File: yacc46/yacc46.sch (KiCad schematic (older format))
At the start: 127 parts, among them J1 CX70M-24P1, J2 OLED_I2C, J3 AVR-ISP-6, J4 GLOVE_I2C, J5 TRRS_I2C, SW1 SW_PUSH, SW10 SW_PUSH, SW11 SW_PUSH, SW12 SW_PUSH, SW13 SW_PUSH, SW14 SW_PUSH, SW15 SW_PUSH, SW16 SW_PUSH, SW17 SW_PUSH, SW18 SW_PUSH, SW19 Rotary_Encoder_Switch, SW2 SW_PUSH, SW20 SW_PUSH, SW21 SW_PUSH, SW22 SW_PUSH, SW23 SW_PUSH, SW24 SW_PUSH, SW25 SW_PUSH, SW26 SW_PUSH, SW27 SW_PUSH, SW28 SW_PUSH, SW29 SW_PUSH, SW3 SW_PUSH, SW30 SW_PUSH, SW31 SW_PUSH, SW32 SW_PUSH, SW33 SW_PUSH, SW34 SW_PUSH, SW35 SW_PUSH, SW36 Rotary_Encoder_Switch, SW37 SW_PUSH, SW38 SW_PUSH, SW39 SW_PUSH, SW4 SW_PUSH, SW40 SW_PUSH, SW41 SW_PUSH, SW42 SW_PUSH, SW43 SW_PUSH, SW44 SW_PUSH, SW45 SW_PUSH, SW46 SW_PUSH, SW47 SW_Push, SW5 SW_PUSH, SW6 SW_PUSH, SW7 SW_PUSH, SW8 SW_PUSH, SW9 SW_PUSH, U1 ATmega32U4-AU, Y1 16MHz

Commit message: リセットスイッチ・水晶のフットプリントを変更
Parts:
- SW47: footprint 1m38_kbd:ResetSW_SKRPABE010 -> 1m38_kbd:SW_PUSH_SMD_TVAF06-A020B-R_HandSolder
- Y1: footprint Crystal:Crystal_SMD_2520-4Pin_2.5x2.0mm -> Crystal:Crystal_SMD_SeikoEpson_FA238-4Pin_3.2x2.5mm_HandSoldering
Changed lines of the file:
@@
 F 0 "SW47" H 3300 6085 50  0000 C CNN
 F 1 "SW_Push" H 3300 5994 50  0000 C CNN
-F 2 "1m38_kbd:ResetSW_SKRPABE010" H 3300 6000 50  0001 C CNN
+F 2 "1m38_kbd:SW_PUSH_SMD_TVAF06-A020B-R_HandSolder" H 3300 6000 50  0001 C CNN
 F 3 "~" H 3300 6000 50  0001 C CNN
 	1    3300 5800
@@
 F 0 "Y1" V 1654 6194 50  0000 L CNN
 F 1 "16MHz" V 1745 6194 50  0000 L CNN
-F 2 "Crystal:Crystal_SMD_2520-4Pin_2.5x2.0mm" H 1700 5950 50  0001 C CNN
+F 2 "Crystal:Crystal_SMD_SeikoEpson_FA238-4Pin_3.2x2.5mm_HandSoldering" H 1700 5950 50  0001 C CNN
 F 3 "~" H 1700 5950 50  0001 C CNN
 	1    1700 5950

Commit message: 配線を修正
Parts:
- removed J5: TRRS_I2C, 1m38_kbd:MJ-4PP-9_1side_no-mask, symbol foostan_kbd:MJ-4PP-9
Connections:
- wire segments 345 -> 338
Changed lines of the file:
@@
 encoding utf-8
 Sheet 1 1
-Title ""
+Title "yacc46"
 Date ""
-Rev ""
+Rev "0.2"
 Comp ""
 Comment1 ""
@@
 U 1 1 5F59CB24
 P 1700 5950
-F 0 "Y1" V 1654 6194 50  0000 L CNN
-F 1 "16MHz" V 1745 6194 50  0000 L CNN
+F 0 "Y1" V 1650 5600 50  0000 L CNN
+F 1 "16MHz" V 1750 5450 50  0000 L CNN
 F 2 "Crystal:Crystal_SMD_SeikoEpson_FA238-4Pin_3.2x2.5mm_HandSoldering" H 1700 5950 50  0001 C CNN
 F 3 "~" H 1700 5950 50  0001 C CNN
 	1    1700 5950
-	0    1    1    0
-$EndComp
-Connection ~ 1700 5800
-Connection ~ 1700 6100
+	0    -1   -1   0
+$EndComp
 Wire Wire Line
 	1050 5150 1150 5150
@@
 Wire Wire Line
 	1450 5150 2000 5150
-Wire Wire Line
-	1450 5800 1700 5800
-Wire Wire Line
-	1450 6100 1700 6100
-Wire Wire Line
-	1700 5800 2000 5800
-Wire Wire Line
-	1700 6100 2000 6100
 Wire Wire Line
 	1050 6300 1500 6300
@@
 	-1   0    0    1
 $EndComp
-$Comp
-L power:GND #PWR0101
-U 1 1 60A4B503
-P 1900 10250
-F 0 "#PWR0101" H 1900 10000 50  0001 C CNN
-F 1 "GND" H 1905 10077 50  0000 C CNN
-F 2 "" H 1900 10250 50  0001 C CNN
-F 3 "" H 1900 10250 50  0001 C CNN
-	1    1900 10250
-	1    0    0    -1
-$EndComp
-Wire Wire Line
-	1500 10250 1900 10250
-$Comp
-L power:VCC #PWR0102
-U 1 1 60A83F5C
-P 1800 10200
-F 0 "#PWR0102" H 1800 10050 50  0001 C CNN
-F 1 "VCC" H 1815 10373 50  0000 C CNN
-F 2 "" H 1800 10200 50  0001 C CNN
-F 3 "" H 1800 10200 50  0001 C CNN
-	1    1800 10200
-	1    0    0    -1
-$EndComp
-Wire Wire Line
-	1500 10300 1800 10300
-Wire Wire Line
-	1800 10300 1800 10200
-Text GLabel 1600 10350 2    50   Input ~ 0
-SCL
-Text GLabel 1600 10450 2    50   Input ~ 0
-SDA
-Wire Wire Line
-	1500 10350 1600 10350
-Wire Wire Line
-	1500 10400 1550 10400
-Wire Wire Line
-	1550 10400 1550 10450
-Wire Wire Line
-	1550 10450 1600 10450
 Text GLabel 11150 4900 1    50   Input ~ 0
 COL0
@@
 Wire Wire Line
 	11150 2600 11150 3400
-$Comp
-L foostan_kbd:MJ-4PP-9 J5
-U 1 1 60A4AE0C
-P 1300 10325
-F 0 "J5" H 1331 10601 50  0000 C CNN
-F 1 "TRRS_I2C" H 1331 10510 50  0000 C CNN
-F 2 "1m38_kbd:MJ-4PP-9_1side_no-mask" H 1575 10500 50  0001 C CNN
-F 3 "~" H 1575 10500 50  0001 C CNN
-	1    1300 10325
-	1    0    0    -1
-$EndComp
 Text GLabel 2800 8900 3    50   Input ~ 0
 SCL
@@
 Wire Wire Line
 	2750 2350 2750 2550
+Wire Wire Line
+	1450 5800 1700 5800
+Wire Wire Line
+	1450 6100 1700 6100
+Connection ~ 1700 6100
+Wire Wire Line
+	1700 6100 2000 6100
+Connection ~ 1700 5800
+Wire Wire Line
+	1700 5800 2000 5800
 $EndSCHEMATC

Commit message: key_arrange.pyを変更、フットプリントの位置を微調整
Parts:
- C1, C2, C3, C4: footprint Capacitor_SMD:C_0805_2012Metric_Pad1.15x1.40mm_HandSolder -> Capacitor_SMD:C_0805_2012Metric_Pad1.18x1.45mm_HandSolder
- C5, C6: footprint Capacitor_SMD:C_0603_1608Metric_Pad1.05x0.95mm_HandSolder -> Capacitor_SMD:C_0603_1608Metric_Pad1.08x0.95mm_HandSolder
- R1, R2, R3, R4, R5, R6: footprint Resistor_SMD:R_0805_2012Metric_Pad1.15x1.40mm_HandSolder -> Resistor_SMD:R_0805_2012Metric_Pad1.20x1.40mm_HandSolder
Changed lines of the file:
@@
 F 0 "R3" V 2743 3450 50  0000 C CNN
 F 1 "22" V 2834 3450 50  0000 C CNN
-F 2 "Resistor_SMD:R_0805_2012Metric_Pad1.15x1.40mm_HandSolder" V 2880 3450 50  0001 C CNN
+F 2 "Resistor_SMD:R_0805_2012Metric_Pad1.20x1.40mm_HandSolder" V 2880 3450 50  0001 C CNN
 F 3 "~" H 2950 3450 50  0001 C CNN
 	1    2950 3450
@@
 F 0 "R1" V 2743 2050 50  0000 C CNN
 F 1 "5.1k" V 2834 2050 50  0000 C CNN
-F 2 "Resistor_SMD:R_0805_2012Metric_Pad1.15x1.40mm_HandSolder" V 2880 2050 50  0001 C CNN
+F 2 "Resistor_SMD:R_0805_2012Metric_Pad1.20x1.40mm_HandSolder" V 2880 2050 50  0001 C CNN
 F 3 "~" H 2950 2050 50  0001 C CNN
 	1    2950 2050
@@
 F 0 "C5" V 1048 5800 50  0000 C CNN
 F 1 "22p" V 1139 5800 50  0000 C CNN
-F 2 "Capacitor_SMD:C_0603_1608Metric_Pad1.05x0.95mm_HandSolder" H 1338 5650 50  0001 C CNN
+F 2 "Capacitor_SMD:C_0603_1608Metric_Pad1.08x0.95mm_HandSolder" H 1338 5650 50  0001 C CNN
 F 3 "~" H 1300 5800 50  0001 C CNN
 	1    1300 5800
@@
 F 0 "C6" V 1048 6100 50  0000 C CNN
 F 1 "22p" V 1139 6100 50  0000 C CNN
-F 2 "Capacitor_SMD:C_0603_1608Metric_Pad1.05x0.95mm_HandSolder" H 1338 5950 50  0001 C CNN
+F 2 "Capacitor_SMD:C_0603_1608Metric_Pad1.08x0.95mm_HandSolder" H 1338 5950 50  0001 C CNN
 F 3 "~" H 1300 6100 50  0001 C CNN
 	1    1300 6100
@@
 F 0 "C4" V 1448 5450 50  0000 C CNN
 F 1 "1u" V 1539 5450 50  0000 C CNN
-F 2 "Capacitor_SMD:C_0805_2012Metric_Pad1.15x1.40mm_HandSolder" H 1738 5300 50  0001 C CNN
+F 2 "Capacitor_SMD:C_0805_2012Metric_Pad1.18x1.45mm_HandSolder" H 1738 5300 50  0001 C CNN
 F 3 "~" H 1700 5450 50  0001 C CNN
 	1    1700 5450
@@
 F 0 "R5" H 3480 5546 50  0000 R CNN
 F 1 "10k" H 3480 5455 50  0000 R CNN
-F 2 "Resistor_SMD:R_0805_2012Metric_Pad1.15x1.40mm_HandSolder" V 3480 5500 50  0001 C CNN
+F 2 "Resistor_SMD:R_0805_2012Metric_Pad1.20x1.40mm_HandSolder" V 3480 5500 50  0001 C CNN
 F 3 "~" H 3550 5500 50  0001 C CNN
 	1    3550 5500
@@
 F 0 "C3" V 1048 5150 50  0000 C CNN
 F 1 "0.1u" V 1139 5150 50  0000 C CNN
-F 2 "Capacitor_SMD:C_0805_2012Metric_Pad1.15x1.40mm_HandSolder" H 1338 5000 50  0001 C CNN
+F 2 "Capacitor_SMD:C_0805_2012Metric_Pad1.18x1.45mm_HandSolder" H 1338 5000 50  0001 C CNN
 F 3 "~" H 1300 5150 50  0001 C CNN
 	1    1300 5150
@@
 F 0 "R6" V 3093 6150 50  0000 C CNN
 F 1 "10k" V 3184 6150 50  0000 C CNN
-F 2 "Resistor_SMD:R_0805_2012Metric_Pad1.15x1.40mm_HandSolder" V 3230 6150 50  0001 C CNN
+F 2 "Resistor_SMD:R_0805_2012Metric_Pad1.20x1.40mm_HandSolder" V 3230 6150 50  0001 C CNN
 F 3 "~" H 3300 6150 50  0001 C CNN
 	1    3300 6150
@@
 F 0 "C1" H 1335 4104 50  0000 R CNN
 F 1 "10u" H 1335 4195 50  0000 R CNN
-F 2 "Capacitor_SMD:C_0805_2012Metric_Pad1.15x1.40mm_HandSolder" H 1488 4000 50  0001 C CNN
+F 2 "Capacitor_SMD:C_0805_2012Metric_Pad1.18x1.45mm_HandSolder" H 1488 4000 50  0001 C CNN
 F 3 "~" H 1450 4150 50  0001 C CNN
 	1    1450 4150
@@
 F 0 "C2" H 1735 4104 50  0000 R CNN
 F 1 "0.1u" H 1735 4195 50  0000 R CNN
-F 2 "Capacitor_SMD:C_0805_2012Metric_Pad1.15x1.40mm_HandSolder" H 1888 4000 50  0001 C CNN
+F 2 "Capacitor_SMD:C_0805_2012Metric_Pad1.18x1.45mm_HandSolder" H 1888 4000 50  0001 C CNN
 F 3 "~" H 1850 4150 50  0001 C CNN
 	1    1850 4150
@@
 F 0 "R4" V 2743 3750 50  0000 C CNN
 F 1 "22" V 2834 3750 50  0000 C CNN
-F 2 "Resistor_SMD:R_0805_2012Metric_Pad1.15x1.40mm_HandSolder" V 2880 3750 50  0001 C CNN
+F 2 "Resistor_SMD:R_0805_2012Metric_Pad1.20x1.40mm_HandSolder" V 2880 3750 50  0001 C CNN
 F 3 "~" H 2950 3750 50  0001 C CNN
 	1    2950 3750
@@
 F 0 "R2" V 643 2350 50  0000 C CNN
 F 1 "5.1k" V 734 2350 50  0000 C CNN
-F 2 "Resistor_SMD:R_0805_2012Metric_Pad1.15x1.40mm_HandSolder" V 780 2350 50  0001 C CNN
+F 2 "Resistor_SMD:R_0805_2012Metric_Pad1.20x1.40mm_HandSolder" V 780 2350 50  0001 C CNN
 F 3 "~" H 850 2350 50  0001 C CNN
 	1    850  2350

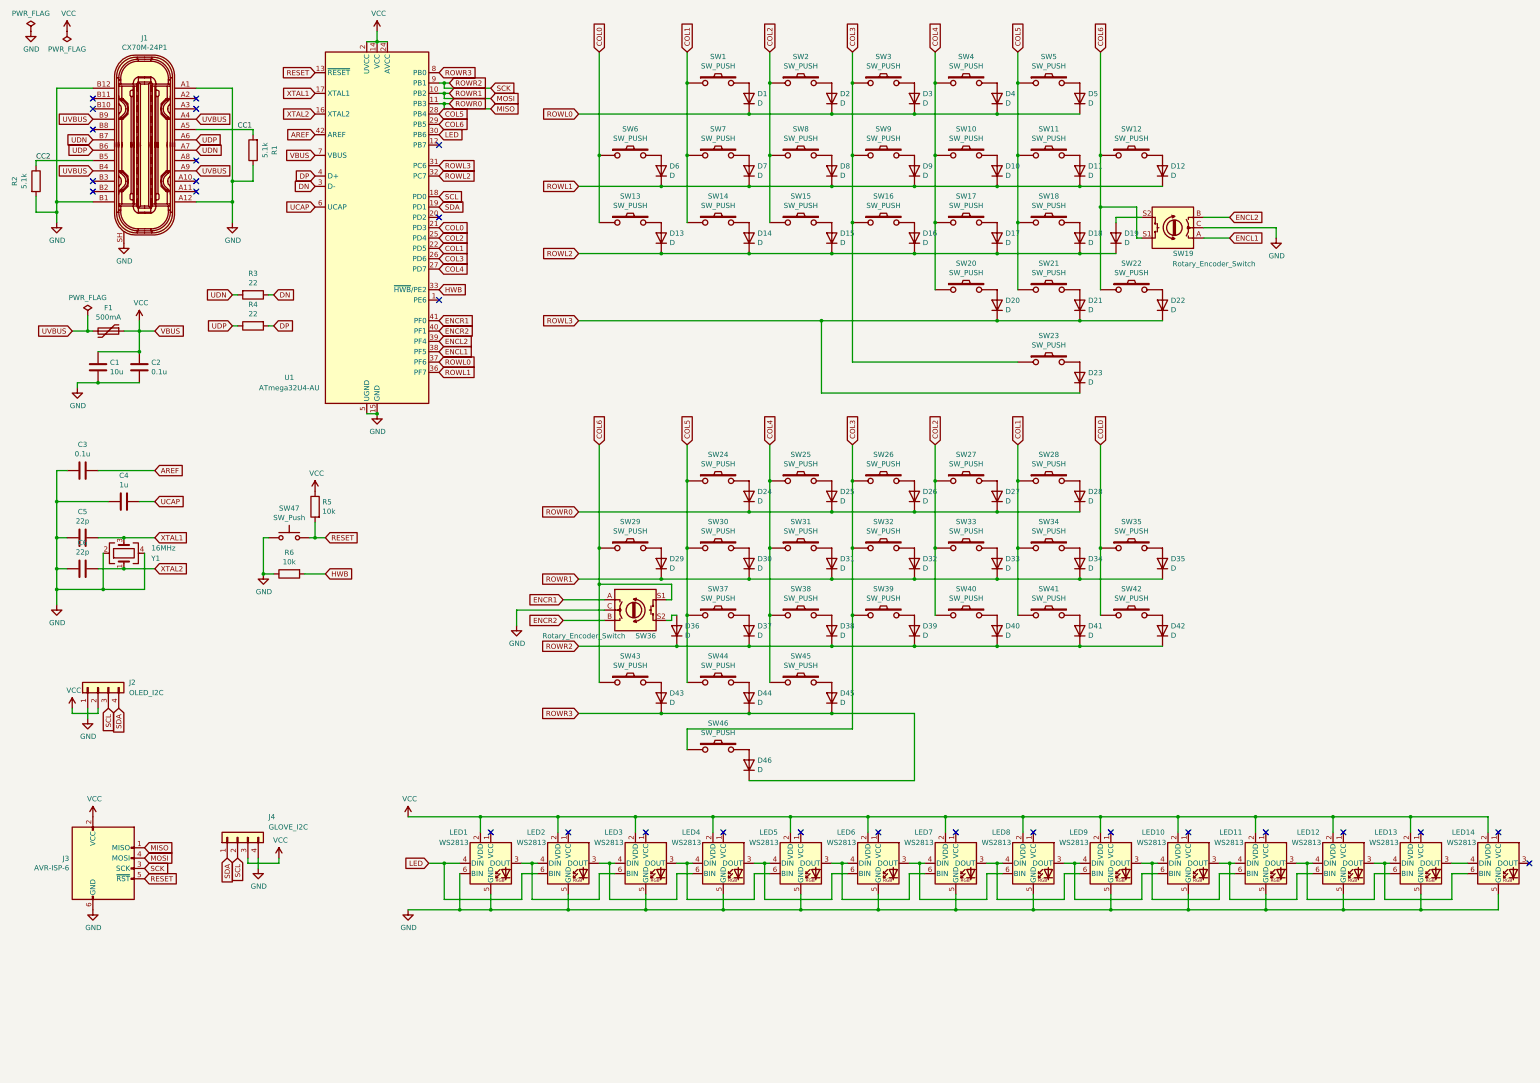
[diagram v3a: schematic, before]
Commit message: yacc46の回路図を修正
- ESD保護ダイオードPRTR5V0U2Xを追加
- USBレセプタクルをCX90M-16Pに変更
- LEDをWS2812Bに変更
- MountingHoleを追加
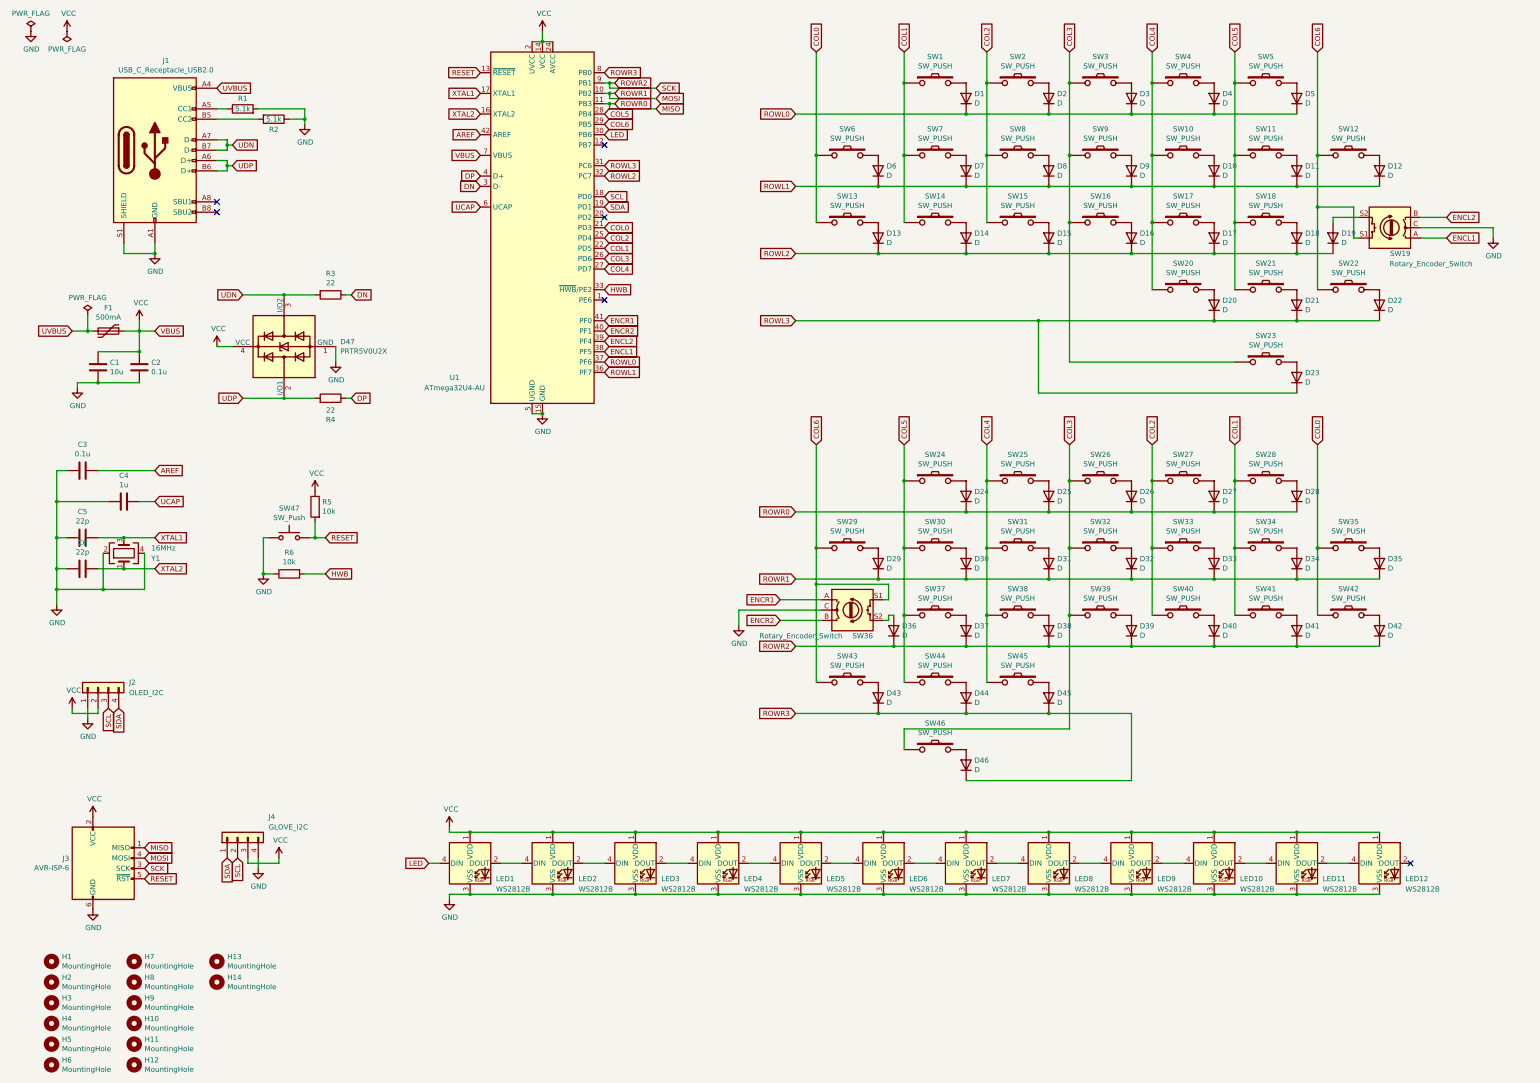
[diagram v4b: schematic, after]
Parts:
- removed J1: CX70M-24P1, digikey-footprints:USB-C_Female_CX70M-24P1, symbol dk_USB-DVI-HDMI-Connectors:CX70M-24P1
- removed LED1, LED10, LED11, LED12, LED13, LED14, LED2, LED3, LED4, LED5, LED6, LED7, LED8, LED9: WS2813, LED_SMD:LED_WS2812_PLCC6_5.0x5.0mm_P1.6mm, symbol LED:WS2813
- added D47: PRTR5V0U2X, Package_TO_SOT_SMD:SOT-143, symbol Power_Protection:PRTR5V0U2X
- added H1, H10, H11, H12, H2, H3, H4, H5, H6, H7, H8, H9: MountingHole, foostan_kbd:M2_HOLE_v2, symbol Mechanical:MountingHole
- added H13, H14: MountingHole, MountingHole:MountingHole_2.2mm_M2, symbol Mechanical:MountingHole
- added J1: USB_C_Receptacle_USB2.0, 1m38_kbd:USB-C_Female_CX90M-16P, symbol Connector:USB_C_Receptacle_USB2.0
- added LED1, LED10, LED11, LED12, LED2, LED3, LED4, LED5, LED6, LED7, LED8, LED9: WS2812B, foostan_kbd:LED_WS2812B-PLCC4, symbol LED:WS2812B
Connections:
- net CC1 is gone; now on net GND: R1.2
- net CC2 is gone; now on net GND: R2.1
- net DP: now also R4.1; no longer R4.2
- net GND: now also D47.1 (GND), J1.A1 (GND), J1.A12 (GND), J1.B1 (GND), J1.B12 (GND), J1.S1 (SHIELD), LED1.3 (VSS), LED10.3 (VSS), LED11.3 (VSS), LED12.3 (VSS), LED2.3 (VSS), LED3.3 (VSS), LED4.3 (VSS), LED5.3 (VSS), LED6.3 (VSS), LED7.3 (VSS), LED8.3 (VSS), LED9.3 (VSS); no longer R1.1, R2.2
- net LED: now also LED1.4 (DIN)
- net UDN: now also D47.3 (I/O2), J1.A7 (D-), J1.B7 (D-)
- net UDP: now also R4.2, D47.2 (I/O1), J1.A6 (D+), J1.B6 (D+); no longer R4.1
- net UVBUS: now also J1.A4 (VBUS), J1.A9 (VBUS), J1.B4 (VBUS), J1.B9 (VBUS)
- net VCC: now also D47.4 (VCC), LED1.1 (VDD), LED10.1 (VDD), LED11.1 (VDD), LED12.1 (VDD), LED2.1 (VDD), LED3.1 (VDD), LED4.1 (VDD), LED5.1 (VDD), LED6.1 (VDD), LED7.1 (VDD), LED8.1 (VDD), LED9.1 (VDD)
- new net: J1.A5 (CC1), R1.1
- new net: J1.B5 (CC2), R2.2
- new net: LED1.2 (DOUT), LED2.4 (DIN)
- new net: LED2.2 (DOUT), LED3.4 (DIN)
- new net: LED3.2 (DOUT), LED4.4 (DIN)
- new net: LED4.2 (DOUT), LED5.4 (DIN)
- new net: LED5.2 (DOUT), LED6.4 (DIN)
- new net: LED6.2 (DOUT), LED7.4 (DIN)
- new net: LED7.2 (DOUT), LED8.4 (DIN)
- new net: LED8.2 (DOUT), LED9.4 (DIN)
- new net: LED10.4 (DIN), LED9.2 (DOUT)
- new net: LED10.2 (DOUT), LED11.4 (DIN)
- new net: LED11.2 (DOUT), LED12.4 (DIN)
- no-connect marks 28 -> 6
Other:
- moved on the sheet: D1, D10, D11, D12, D13, D14, D15, D16, D17, D18, D19, D2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
